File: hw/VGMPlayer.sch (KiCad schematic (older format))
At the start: 96 parts, among them J1 Micro_SD_Card, J2 EarPiece, M1 Mechanical-NC, P1 USB_C_Receptacle_16P, P2 SWD, P3 BATT, P5 ICSP, P6 CODEC, Q1 AO3401A, Q2 AO3401A, Q3 2N7002, Q4 2N7002, U1 RP2040, U2 W25QxxJVZP, U3 LP5907MFX-3.3, U4 WM8978, U5 MCP73831-OT, U6 PIC16F1503-IMG, U7 LP5907MFX-3.3, Y1 12MHz

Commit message: Change 2N7002 footprint to SOT-523
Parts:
- Q3, Q4: footprint BZ_Standard_IC:SOT-323-3 -> BZ_Standard_IC:SOT-523
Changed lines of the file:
@@
 F 0 "Q4" H 8800 1750 40  0000 L CNN
 F 1 "2N7002" H 8750 1400 40  0000 L CNN
-F 2 "BZ_Standard_IC:SOT-323-3" H 8900 1600 40  0001 C CNN
+F 2 "BZ_Standard_IC:SOT-523" H 8900 1600 40  0001 C CNN
 F 3 "" H 8900 1600 40  0001 C CNN
 	1    8900 1600
@@
 F 0 "Q3" H 4250 2700 40  0000 L CNN
 F 1 "2N7002" H 4250 2600 40  0000 L CNN
-F 2 "BZ_Standard_IC:SOT-323-3" H 4050 2650 40  0001 C CNN
+F 2 "BZ_Standard_IC:SOT-523" H 4050 2650 40  0001 C CNN
 F 3 "" H 4050 2650 40  0001 C CNN
 	1    4050 2650
@@
 BATT
 $Comp
-L BZ_Switch:PB-SPST-NO_2P S4
-U 1 1 61B88515
-P 1700 2350
-F 0 "S4" H 1550 2400 40  0000 C CNN
-F 1 "D" H 1800 2400 40  0000 L CNN
-F 2 "BZ_Switch:C&K_PTS525" H 1700 2350 40  0001 C CNN
-F 3 "" H 1700 2350 40  0001 C CNN
-	1    1700 2350
-	1    0    0    -1
-$EndComp
-$Comp
 L BZ_Power:GND #PWR0114
 U 1 1 61B88737
@@
 $EndComp
 Wire Wire Line
+	1300 1650 1650 1650
+Wire Wire Line
+	1300 1650 1300 2650
+Wire Wire Line
+	1850 2350 2200 2350
+Wire Wire Line
+	1450 2350 1450 2450
+Wire Wire Line
 	1450 2250 1450 2350
-Wire Wire Line
-	1300 1650 1650 1650
-Wire Wire Line
-	1850 2350 2200 2350
+Connection ~ 1450 2350
 Wire Wire Line
 	1550 2350 1450 2350
-Connection ~ 1450 2350
-Wire Wire Line
-	1450 2350 1450 2450
 Wire Wire Line
 	1450 2550 1450 2700
+$Comp
+L BZ_Switch:PB-SPST-NO_2P S4
+U 1 1 61B88515
+P 1700 2350
+F 0 "S4" H 1550 2400 40  0000 C CNN
+F 1 "D" H 1800 2400 40  0000 L CNN
+F 2 "BZ_Switch:C&K_PTS525" H 1700 2350 40  0001 C CNN
+F 3 "" H 1700 2350 40  0001 C CNN
+	1    1700 2350
+	1    0    0    -1
+$EndComp
 Wire Wire Line
 	1300 2650 2200 2650
-Wire Wire Line
-	1300 1650 1300 2650
 $EndSCHEMATC

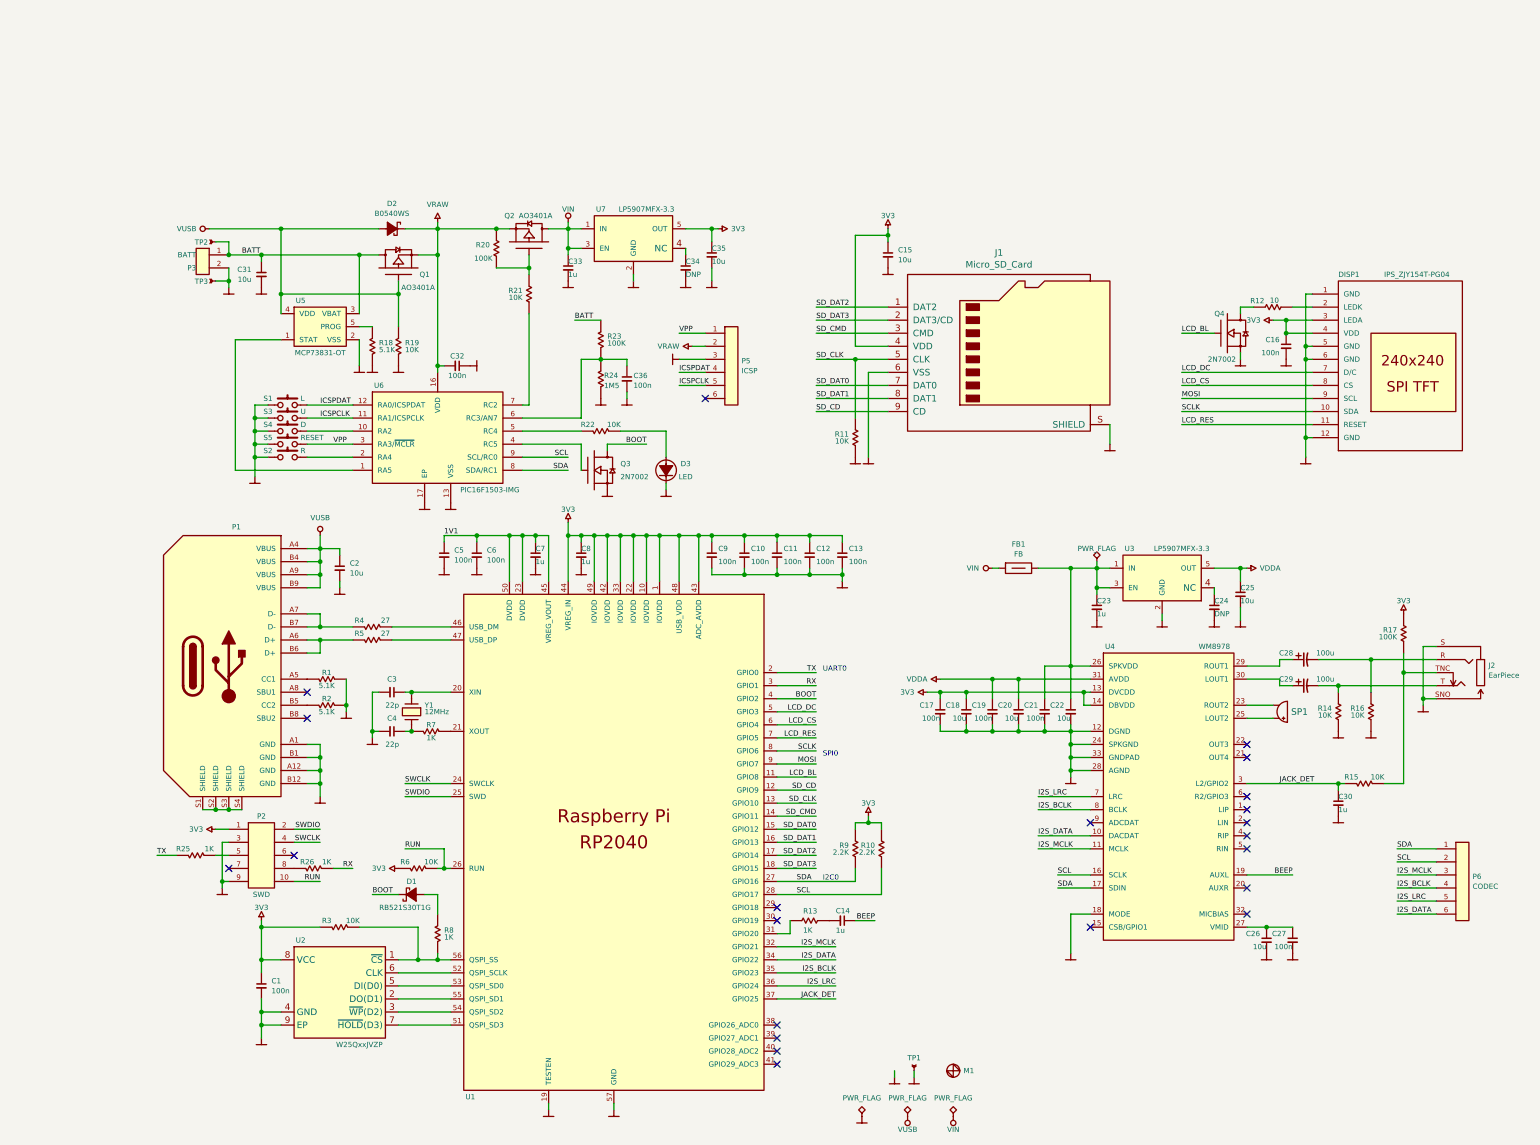
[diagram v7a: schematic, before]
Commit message: Fix SWD connector orientation
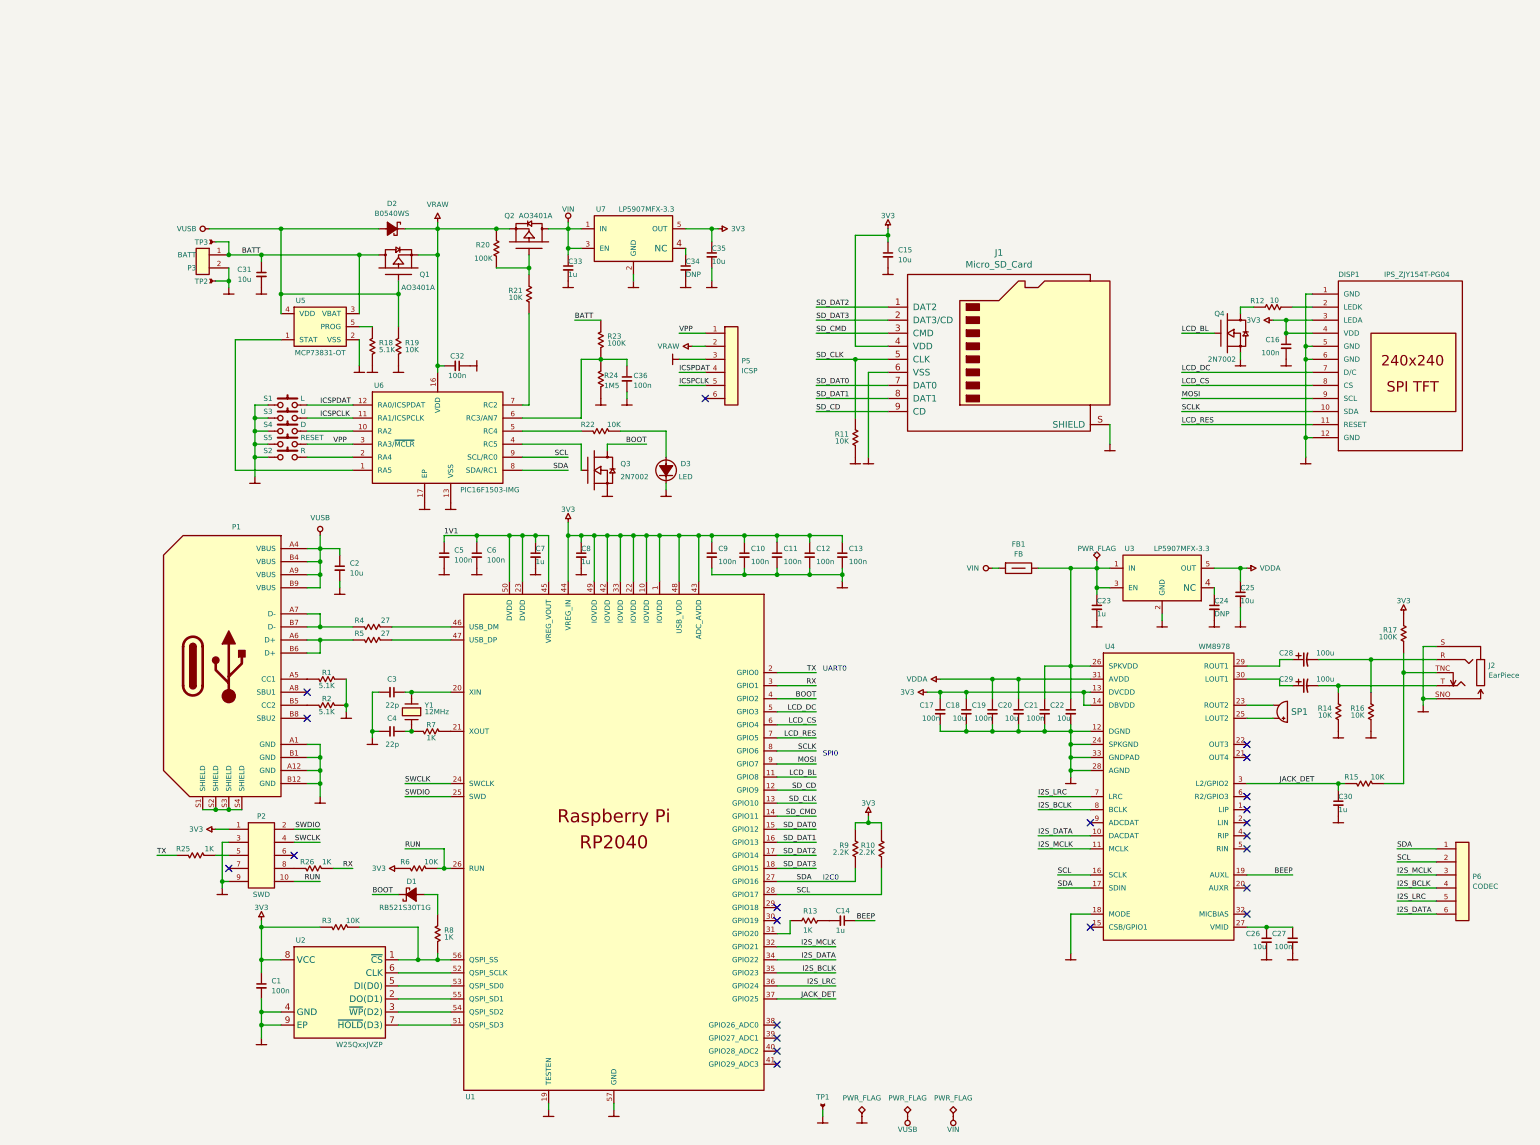
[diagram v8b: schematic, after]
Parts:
- removed M1: Mechanical-NC, BZ_Mechanical:Hole-Mech_0.5, symbol BZ_Misc:Mechanical-NC
- renumbered TP3 to TP2, TP2 to TP3
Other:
- moved on the sheet: TP1
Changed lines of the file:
@@
 L BZ_Misc:TP TP1
 U 1 1 60BC7B96
-P 6500 7250
-F 0 "TP1" H 6500 7325 40  0000 C BNN
-F 1 "TP" H 6500 7200 40  0001 C CNN
-F 2 "BZ_Misc:TP_THT-Pad-0.8" H 6500 7250 40  0001 C CNN
-F 3 "" H 6500 7250 40  0001 C CNN
-	1    6500 7250
+P 5800 7550
+F 0 "TP1" H 5800 7625 40  0000 C BNN
+F 1 "TP" H 5800 7500 40  0001 C CNN
+F 2 "BZ_Misc:TP_THT-Pad-0.8" H 5800 7550 40  0001 C CNN
+F 3 "" H 5800 7550 40  0001 C CNN
+	1    5800 7550
 	1    0    0    -1
 $EndComp
@@
 L BZ_Power:GND #PWR0107
 U 1 1 60BC86BB
-P 6500 7300
-F 0 "#PWR0107" H 6500 7300 30  0001 C CNN
-F 1 "GND" H 6500 7230 30  0001 C CNN
-F 2 "" H 6500 7300 60  0001 C CNN
-F 3 "" H 6500 7300 60  0001 C CNN
-	1    6500 7300
-	1    0    0    -1
-$EndComp
-Wire Wire Line
-	6500 7300 6500 7250
+P 5800 7600
+F 0 "#PWR0107" H 5800 7600 30  0001 C CNN
+F 1 "GND" H 5800 7530 30  0001 C CNN
+F 2 "" H 5800 7600 60  0001 C CNN
+F 3 "" H 5800 7600 60  0001 C CNN
+	1    5800 7600
+	1    0    0    -1
+$EndComp
+Wire Wire Line
+	5800 7600 5800 7550
 Wire Wire Line
 	8800 3400 9000 3400
@@
 	1850 2450 2200 2450
 $Comp
-L BZ_Misc:TP TP2
+L BZ_Misc:TP TP3
 U 1 1 6150793C
 P 1150 900
-F 0 "TP2" V 1170 1010 40  0000 C BNN
+F 0 "TP3" V 1170 1010 40  0000 C BNN
 F 1 "TP" H 1150 850 40  0001 C CNN
 F 2 "BZ_Misc:TP_THT-Pad-0.8" H 1150 900 40  0001 C CNN
@@
 $EndComp
 $Comp
-L BZ_Misc:TP TP3
+L BZ_Misc:TP TP2
 U 1 1 61507D48
 P 1150 1200
-F 0 "TP3" V 1170 1310 40  0000 C BNN
+F 0 "TP2" V 1170 1310 40  0000 C BNN
 F 1 "TP" H 1150 1150 40  0001 C CNN
 F 2 "BZ_Misc:TP_THT-Pad-0.8" H 1150 1200 40  0001 C CNN
@@
 	0    -1   -1   0
 $EndComp
-$Comp
-L BZ_Power:GND #PWR0112
-U 1 1 6155A872
-P 6350 7300
-F 0 "#PWR0112" H 6350 7300 30  0001 C CNN
-F 1 "GND" H 6350 7230 30  0001 C CNN
-F 2 "" H 6350 7300 60  0001 C CNN
-F 3 "" H 6350 7300 60  0001 C CNN
-	1    6350 7300
-	1    0    0    -1
-$EndComp
-Wire Wire Line
-	6350 7300 6350 7250
 $Comp
 L BZ_Microchip:MCP73831-OT U5
@@
 	1    0    0    -1
 $EndComp
-$Comp
-L BZ_Misc:Mechanical-NC M1
-U 1 1 61666DF3
-P 6800 7250
-F 0 "M1" H 6878 7250 40  0000 L CNN
-F 1 "Mechanical-NC" H 6800 7250 40  0001 C CNN
-F 2 "BZ_Mechanical:Hole-Mech_0.5" H 6800 7250 50  0001 C CNN
-F 3 "" H 6800 7250 50  0001 C CNN
-	1    6800 7250
-	1    0    0    -1
-$EndComp
